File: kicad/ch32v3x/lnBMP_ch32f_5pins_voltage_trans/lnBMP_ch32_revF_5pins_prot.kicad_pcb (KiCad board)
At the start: 2 copper layers, 51 x 33.3 mm, 53 parts, among them J1 Conn_ARM_JTAG_SWD_10, J3 Debug port, J4 USB_C_Receptacle, J5 Debug port, U1 CH32V303RCT6, U2 LM1117-3.3, Y1 Crystal, x2 PinSocket_1x03_P1.00mm_Vertic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

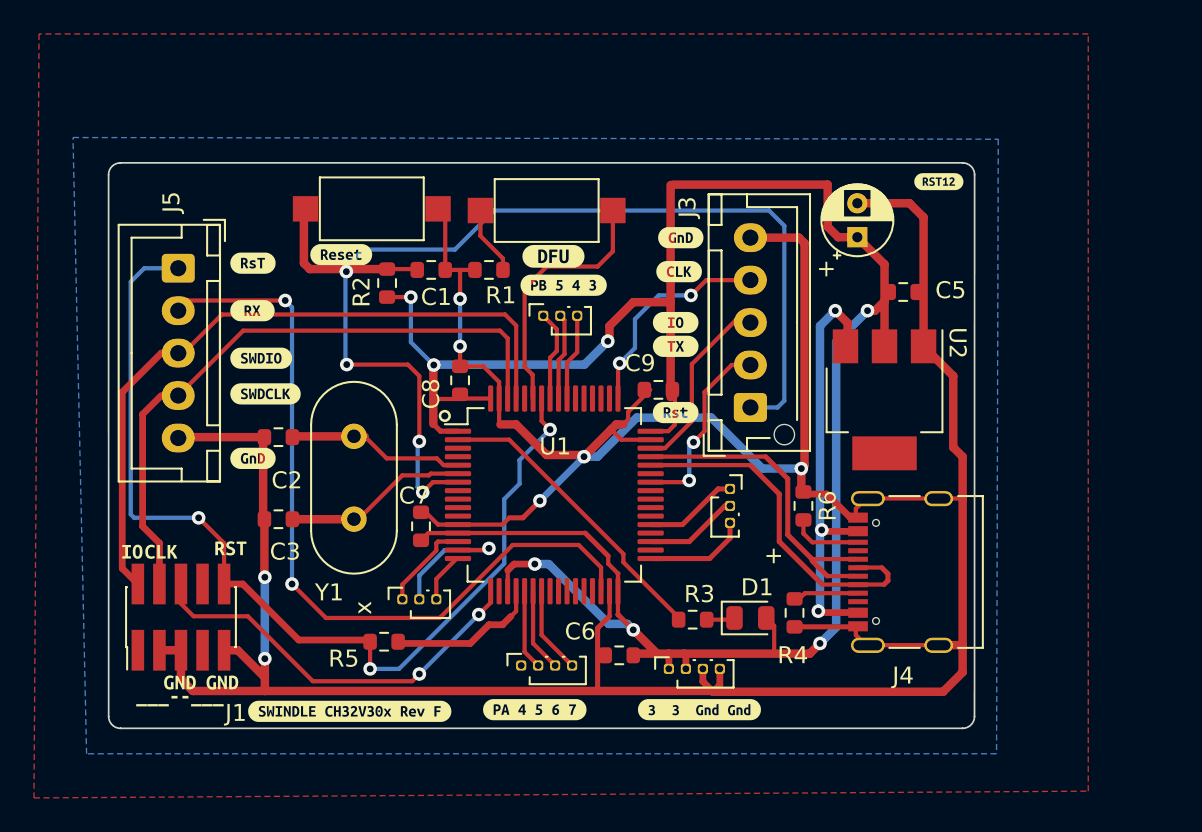
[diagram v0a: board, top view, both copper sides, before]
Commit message: add level shifter
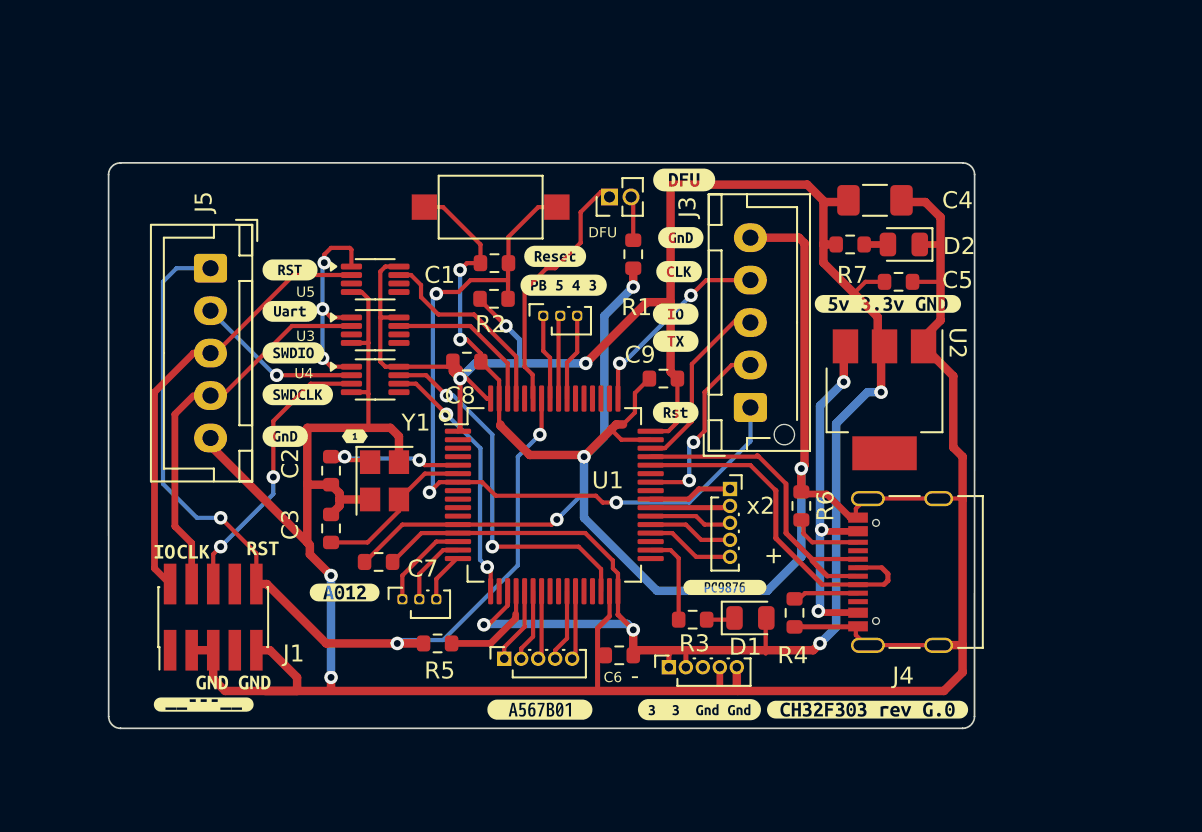
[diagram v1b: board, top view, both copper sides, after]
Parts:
- removed DFU1: SWDFU, Button_Switch_SMD:SW_SPST_CK_RS282G05A3
- removed kibuzzard-65C13741: G***, kibuzzard-65C13741
- removed kibuzzard-65C1C718: G***, kibuzzard-65C1C718
- removed kibuzzard-65C1C7A6: G***, kibuzzard-65C1C7A6
- removed kibuzzard-65C281E1: G***, kibuzzard-65C281E1
- removed kibuzzard-65D842E2: G***, kibuzzard-65D842E2
- removed kibuzzard-66C043C9: G***, kibuzzard-66C043C9
- added D2: LED, Diode_SMD:D_0805_2012Metric, F.Cu at (151.1, 71.7)
- added DFU: Conn_01x02_Pin, Connector_PinHeader_1.27mm:PinHeader_1x02_P1.27mm_Vertical, F.Cu at (133.8, 68.9)
- added R7: 330, Resistor_SMD:R_0603_1608Metric, F.Cu at (148.0, 71.7)
- added U3: 3V->VTREF, Package_SO:VSSOP-8_2.3x2mm_P0.5mm, F.Cu at (120.0, 76.8)
- added U4: VTREF->3V, Package_SO:VSSOP-8_2.3x2mm_P0.5mm, F.Cu at (120.0, 79.7)
- added U5: VTREF<->3V, Package_SO:VSSOP-8_2.3x2mm_P0.5mm, F.Cu at (120.0, 73.8)
- added kibuzzard-6711F463: G***, kibuzzard-6711F463, F.Cu at (149.0, 99.1)
- added kibuzzard-67135D50: G***, kibuzzard-67135D50, F.Cu at (150.2, 75.2)
- added kibuzzard-67135D9A: G***, kibuzzard-67135D9A, F.Cu at (118.2, 92.2)
- added kibuzzard-67135DB6: G***, kibuzzard-67135DB6, F.Cu at (109.9, 98.8)
- added kibuzzard-671361D3: G***, kibuzzard-671361D3, F.Cu at (118.8, 83.0)
- added kibuzzard-67137B47: G***, kibuzzard-67137B47, F.Cu at (115.0, 73.2)
- added kibuzzard-67137B7B: G***, kibuzzard-67137B7B, F.Cu at (115.0, 75.6)
- added kibuzzard-6713D043: G***, kibuzzard-6713D043, F.Cu at (140.6, 91.9)
- added kibuzzard-6713D917: G***, kibuzzard-6713D917, F.Cu at (129.7, 99.1)
- -: renamed from 3/3/GND/GND; value PinSocket_1x04_P1.00mm_Vertical -> PinSocket_1x05_P1.00mm_Vertical; footprint Connector_PinSocket_1.00mm:PinSocket_1x04_P1.00mm_Vertical -> Connector_PinSocket_1.00mm:PinSocket_1x05_P1.00mm_Vertical
- C2, C3: value 10pf -> 22pf
- C4: footprint Capacitor_THT:CP_Radial_D4.0mm_P2.00mm -> Capacitor_SMD:C_1206_3216Metric_Pad1.33x1.80mm_HandSolder
- PA4567: value PinSocket_1x04_P1.00mm_Vertical -> PinSocket_1x05_P1.00mm_Vertical; footprint Connector_PinSocket_1.00mm:PinSocket_1x04_P1.00mm_Vertical -> Connector_PinSocket_1.00mm:PinSocket_1x05_P1.00mm_Vertical
- Y1: value Crystal -> 8Mhz; footprint Crystal:Crystal_HC49-U_Vertical -> Crystal:Crystal_SMD_TXC_7M-4Pin_3.2x2.5mm
- x2: value PinSocket_1x03_P1.00mm_Vertical -> PinSocket_1x05_P1.00mm_Vertical; footprint Connector_PinSocket_1.00mm:PinSocket_1x03_P1.00mm_Vertical -> Connector_PinSocket_1.00mm:PinSocket_1x05_P1.00mm_Vertical
- moved kibuzzard-65C1C9D7 12.6 mm to (130.6, 72.4)
- moved kibuzzard-664C331A 8.92 mm to (138.2, 67.9)
- moved R1 8.55 mm to (135.2, 72.3), turned to -90 degrees
- moved RST1 7.00 mm to (126.8, 69.5), turned to 180 degrees
- moved R2 6.37 mm to (127.0, 74.9), turned to 0 degrees
- moved C1 3.75 mm to (127.0, 72.8), turned to 180 degrees
- moved C2 3.68 mm to (117.4, 85.0), turned to -90 degrees
- moved C7 3.26 mm to (120.2, 90.4), turned to 180 degrees
- moved Y1 3.18 mm to (120.5, 85.6), turned to 180 degrees
- moved R5 3.15 mm to (123.7, 95.2)
- moved C3 3.15 mm to (117.4, 88.4), turned to 90 degrees
- moved C4 2.41 mm to (149.4, 69.1), turned to 0 degrees
- moved kibuzzard-65C1C789 2.30 mm to (114.7, 83.0)
- moved kibuzzard-65C1C7F5 1.93 mm to (115.2, 78.1)
- moved kibuzzard-65C1C805 1.90 mm to (115.4, 80.5)
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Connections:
- - pad 3: GND -> (no net)
- PA4567 pad 1: unconnected-(U1-PA4-Pad20) -> unconnected-(U1-PA5-Pad21)
- PA4567 pad 2: unconnected-(U1-PA5-Pad21) -> unconnected-(U1-PA6-Pad22)
- PA4567 pad 3: unconnected-(U1-PA6-Pad22) -> unconnected-(U1-PA7-Pad23)
- PA4567 pad 4: unconnected-(U1-PA7-Pad23) -> unconnected-(U1-PB0-Pad26)
- R3 pad 1: Net-(U1-PC13) -> Net-(D1-K)
- R3 pad 2: Net-(D1-K) -> Net-(U1-PB13)
- U1 pad 17: INOUT_SWO -> INOUT_SWO_3v
- U1 pad 2: Net-(U1-PC13) -> unconnected-(U1-PC13-Pad2)
- U1 pad 30: OUT_UART_RX -> OUT_UART_RX_3V
- U1 pad 34: unconnected-(U1-PB13-Pad34) -> Net-(U1-PB13)
- U1 pad 61: OUT_SWDIO -> OUT_SWDIO_3V
- U1 pad 62: OUT_SWDCLK -> OUT_SWDCLK_3V
- Y1 pad 2: Net-(U1-PF1) -> GND
- x2 pad 1: unconnected-(U1-PC6-Pad37) -> unconnected-(U1-PC9-Pad40)
- x2 pad 2: unconnected-(U1-PB14-Pad35) -> unconnected-(U1-PC8-Pad39)
- x2 pad 3: unconnected-(U1-PB12-Pad33) -> unconnected-(U1-PC7-Pad38)
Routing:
- net GND: track 208.6 -> 265.4 mm, vias 7 -> 8
- net OUT_UART_RX: track 46.2 -> 10.1 mm, vias 2 -> 1
- net NRESET: track 69.6 -> 46.2 mm, vias 4 -> 3
- net OUT_UART_RX_3V: track 0.00 -> 21.7 mm, vias 0 -> 2
- net Net-(U1-PC13): track 17.6 -> 0.00 mm
- net OUT_SWDCLK: track 37.8 -> 22.3 mm
- net OUT_SWDIO: track 41.0 -> 25.8 mm
- net INOUT_SWO_3v: track 0.00 -> 15.1 mm, vias 0 -> 2
- net VTREF: track 0.00 -> 12.8 mm, vias 0 -> 3
- net OUT_SWDIO_3V: track 0.00 -> 11.8 mm
- net +3.3V: track 133.1 -> 143.9 mm
- net OUT_SWDCLK_3V: track 0.00 -> 9.39 mm
- net INOUT_SWO: track 23.9 -> 16.6 mm
- net unconnected-(U1-PB12-Pad33): track 6.07 -> 0.00 mm
- net unconnected-(U1-PB14-Pad35): track 5.54 -> 0.00 mm
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- removed copper zone on B.Cu, net GND
- removed copper zone on F.Cu, net GND

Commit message: CH32:; add voltage shifter  (cont)
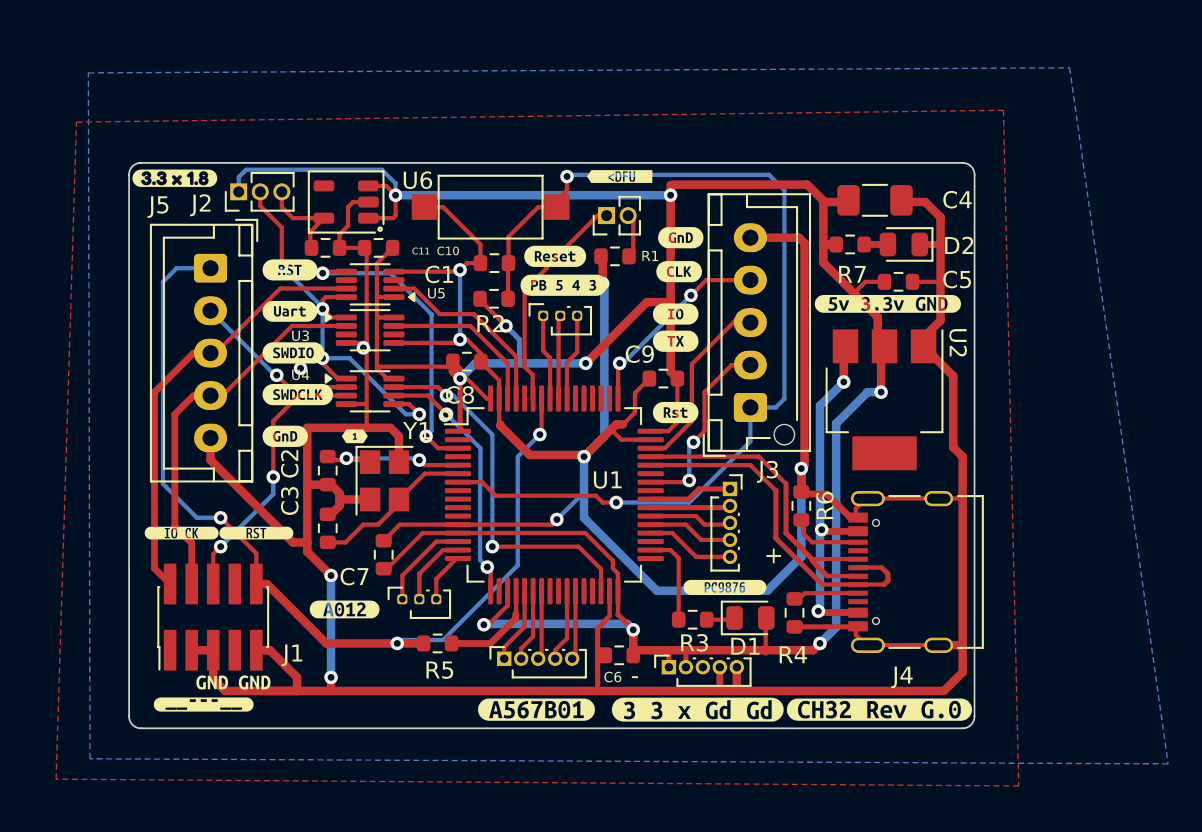
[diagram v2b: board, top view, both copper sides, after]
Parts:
- removed kibuzzard-65C281F8: G***, kibuzzard-65C281F8
- removed kibuzzard-664C331A: G***, kibuzzard-664C331A
- removed kibuzzard-66C04316: G***, kibuzzard-66C04316
- removed kibuzzard-66C04342: G***, kibuzzard-66C04342
- removed kibuzzard-66C0434B: G***, kibuzzard-66C0434B
- removed kibuzzard-6711F463: G***, kibuzzard-6711F463
- removed kibuzzard-6713D917: G***, kibuzzard-6713D917
- added C10: 100n, Resistor_SMD:R_0603_1608Metric, F.Cu at (120.2, 71.9)
- added C11: 100n, Resistor_SMD:R_0603_1608Metric, F.Cu at (117.1, 71.9)
- added J2: Conn_01x03_Socket, Connector_PinHeader_1.27mm:PinHeader_1x03_P1.27mm_Vertical, F.Cu at (112.0, 68.6)
- added U6: RT9013-33GB, PCM_Package_TO_SOT_SMD_AKL:TSOT-23-5, F.Cu at (118.3, 69.2)
- added kibuzzard-6713DC16: G***, kibuzzard-6713DC16, F.Cu at (113.0, 88.7)
- added kibuzzard-6713DC2E: G***, kibuzzard-6713DC2E, F.Cu at (108.6, 88.7)
- added kibuzzard-6714B049: G***, kibuzzard-6714B049, F.Cu at (134.4, 67.7)
- added kibuzzard-6714FCCA: G***, kibuzzard-6714FCCA, F.Cu at (108.2, 67.8)
- added kibuzzard-6714FD27: G***, kibuzzard-6714FD27, F.Cu at (129.5, 99.1)
- added kibuzzard-6714FD4B: G***, kibuzzard-6714FD4B, F.Cu at (139.0, 99.1)
- added kibuzzard-6714FD63: G***, kibuzzard-6714FD63, F.Cu at (149.7, 99.1)
- J1: value Conn_ARM_JTAG_SWD_10 -> jtag
- J2_DFU1: renamed from DFU; value Conn_01x02_Pin -> con2
- J4: value USB_C_Receptacle -> USB
- moved J2_DFU1 1.11 mm to (133.6, 70.0)
- moved R1 1.08 mm to (134.1, 72.4), turned to 180 degrees
- moved kibuzzard-67135D9A 1.00 mm to (118.2, 93.2)
- moved U4 0.76 mm to (119.7, 80.3)
- moved C7 0.52 mm to (120.5, 90.0), turned to 90 degrees
- moved U5 0.42 mm to (119.7, 74.0), turned to 180 degrees
- moved U3 0.30 mm to (119.7, 76.8)
- moved C2 0.20 mm to (117.2, 85.0)
- moved C3 0.20 mm to (117.2, 88.4)
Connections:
- U1 pad 3: unconnected-(U1-PC14-Pad3) -> SWIO_DIR_3V
- U3 pad 5: unconnected-(U3-DIR-Pad5) -> GND
- U4 pad 5: unconnected-(U4-DIR-Pad5) -> VTREF
- U5 pad 1: VTREF -> +3.3V
- U5 pad 2: OUT_SWDIO -> OUT_SWDIO_3V
- U5 pad 5: unconnected-(U5-DIR-Pad5) -> SWIO_DIR_3V
- U5 pad 7: OUT_SWDIO_3V -> OUT_SWDIO
- U5 pad 8: +3.3V -> VTREF
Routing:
- net +3.3V: track 143.9 -> 179.6 mm, vias 7 -> 9
- net SWIO_DIR_3V: track 0.00 -> 18.3 mm, vias 0 -> 2
- net GND: track 265.4 -> 278.4 mm, vias 8 -> 10
- net VTREF: track 12.8 -> 25.3 mm, vias 3 -> 4
- net NRESET: track 46.2 -> 57.3 mm, vias 3 -> 2
- net V1.8: track 0.00 -> 5.66 mm
- net IN_FORCE_DFU: track 15.0 -> 13.3 mm
- net OUT_SWDIO: track 25.8 -> 25.2 mm
- net Net-(U1-PF1): track 9.56 -> 9.06 mm
- added copper zone on B.Cu, net GND
- added copper zone on F.Cu, net GND
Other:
- board size 51 x 33.3 mm -> 49.8 x 33.3 mm
